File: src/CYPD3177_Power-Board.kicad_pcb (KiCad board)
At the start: 2 copper layers, 100 x 100 mm, 1 part

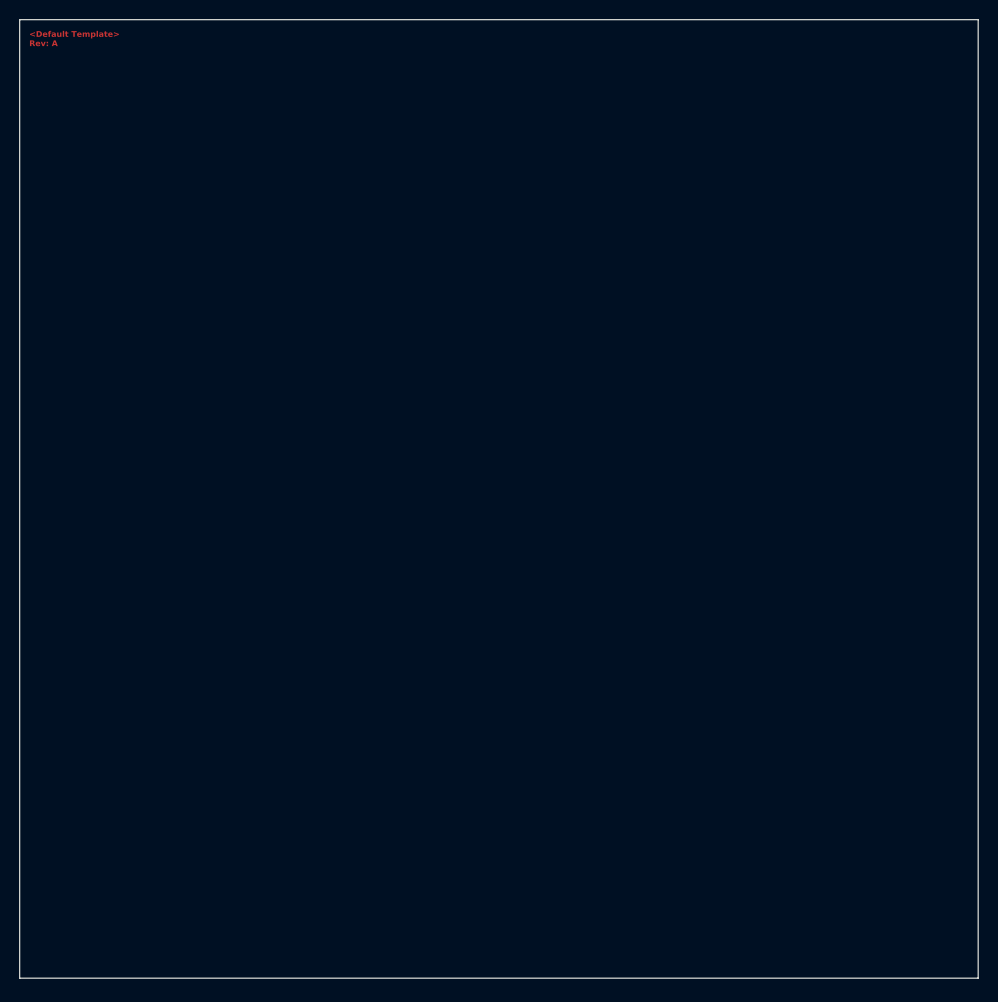
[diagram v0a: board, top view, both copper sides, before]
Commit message: Mod: PCB, placed components, draw board shape and placed a few traces
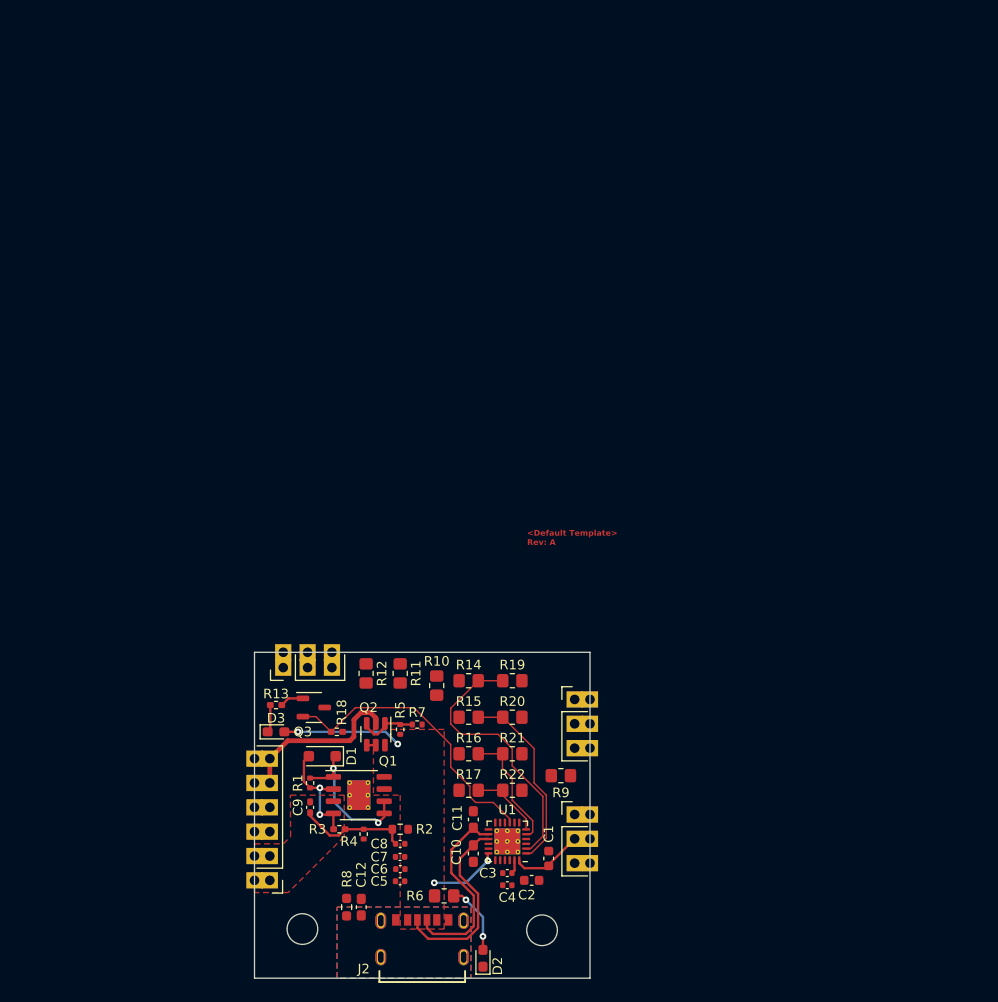
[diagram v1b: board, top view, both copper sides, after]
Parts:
- added C1: 1µF, Capacitor_SMD:C_0603_1608Metric, F.Cu at (155.2, 127.5)
- added C10: 390pF, Capacitor_SMD:C_0603_1608Metric_Pad1.08x0.95mm_HandSolder, F.Cu at (147.3, 127.0)
- added C11: 390pF, Capacitor_SMD:C_0603_1608Metric_Pad1.08x0.95mm_HandSolder, F.Cu at (147.3, 123.4)
- added C12: 4.7nF, Capacitor_SMD:C_0603_1608Metric_Pad1.08x0.95mm_HandSolder, F.Cu at (135.6, 132.6)
- added C2: 1µF, Capacitor_SMD:C_0603_1608Metric, F.Cu at (153.4, 129.8)
- added C3: 0.1µF, Capacitor_SMD:C_0402_1005Metric, F.Cu at (150.9, 129.0)
- added C4: 0.1µF, Capacitor_SMD:C_0402_1005Metric, F.Cu at (150.9, 130.3)
- added C5: 1µF, Capacitor_SMD:C_0402_1005Metric, F.Cu at (139.7, 129.9)
- added C6: 1µF, Capacitor_SMD:C_0402_1005Metric, F.Cu at (139.7, 128.6)
- added C7: 1µF, Capacitor_SMD:C_0402_1005Metric, F.Cu at (139.7, 127.3)
- added C8: 1µF, Capacitor_SMD:C_0402_1005Metric, F.Cu at (139.7, 126.0)
- added C9: 1µF, Capacitor_SMD:C_0402_1005Metric_Pad0.74x0.62mm_HandSolder, F.Cu at (130.3, 122.2)
- added D1: NZH10C,115, Diode_SMD:D_SOD-123F, F.Cu at (131.6, 116.8)
- added D2: LTST-C190GKT, LED_SMD:LED_0603_1608Metric_Pad1.05x0.95mm_HandSolder, F.Cu at (148.3, 137.9)
- added D3: LTST-C190EKT, LED_SMD:LED_0603_1608Metric_Pad1.05x0.95mm_HandSolder, F.Cu at (126.7, 114.3)
- added H1: MountingHole, MountingHole:MountingHole_3.2mm_M3, F.Cu at (129.5, 134.9)
- added H2: MountingHole, MountingHole:MountingHole_3.2mm_M3, F.Cu at (154.5, 135.0)
- added J1: Conn_01x06, Connector_CastellatedHole_2.54mm_User:CastellatedHole_1x06_P2.54mm_PinHeaders, F.Cu at (124.5, 129.8)
- added J2: USB4125-GF-A, Connector_User:GCT_USB4125-GF-A, F.Cu at (142.0, 137.0)
- added J3: Conn_01x03, Connector_CastellatedHole_2.54mm_User:CastellatedHole_1x03_P2.54mm_PinHeader, F.Cu at (159.5, 122.9)
- added J4: Conn_01x03, Connector_CastellatedHole_2.54mm_User:CastellatedHole_1x03_P2.54mm_PinHeader, F.Cu at (127.5, 106.0)
- added J5: Conn_01x03, Connector_CastellatedHole_2.54mm_User:CastellatedHole_1x03_P2.54mm_PinHeader, F.Cu at (159.5, 110.9)
- added Q1: IRF9358PbF, Package_SO:HSOP-8-1EP_3.9x4.9mm_P1.27mm_EP2.41x3.1mm_ThermalVias, F.Cu at (135.4, 120.9)
- added Q2: BSL308PE, Package_TO_SOT_SMD:SOT-23-6, F.Cu at (137.2, 114.6)
- added Q3: NTR4503N, Package_TO_SOT_SMD:SOT-23-3, F.Cu at (130.7, 111.8)
- added R1: 49.9kΩ, Resistor_SMD:R_0402_1005Metric, F.Cu at (130.3, 119.6)
- added R10: 2.2kΩ, Resistor_SMD:R_0805_2012Metric_Pad1.20x1.40mm_HandSolder, F.Cu at (143.5, 109.5)
- added R11: 2.2kΩ, Resistor_SMD:R_0805_2012Metric_Pad1.20x1.40mm_HandSolder, F.Cu at (139.7, 108.2)
- added R12: 2.2kΩ, Resistor_SMD:R_0805_2012Metric_Pad1.20x1.40mm_HandSolder, F.Cu at (136.1, 108.2)
- added R13: 1kΩ, Resistor_SMD:R_0402_1005Metric_Pad0.72x0.64mm_HandSolder, F.Cu at (126.7, 111.5)
- added R14: 5.1kΩ, Resistor_SMD:R_0805_2012Metric_Pad1.20x1.40mm_HandSolder, F.Cu at (146.8, 109.0)
- added R15: 5.1kΩ, Resistor_SMD:R_0805_2012Metric_Pad1.20x1.40mm_HandSolder, F.Cu at (146.8, 112.8)
- added R16: 5.1kΩ, Resistor_SMD:R_0805_2012Metric_Pad1.20x1.40mm_HandSolder, F.Cu at (146.8, 116.6)
- added R17: 5.1kΩ, Resistor_SMD:R_0805_2012Metric_Pad1.20x1.40mm_HandSolder, F.Cu at (146.8, 120.4)
- added R18: 49.9kΩ, Resistor_SMD:R_0402_1005Metric_Pad0.72x0.64mm_HandSolder, F.Cu at (133.1, 114.3)
- added R19: 5.1kΩ, Resistor_SMD:R_0805_2012Metric_Pad1.20x1.40mm_HandSolder, F.Cu at (151.4, 109.0)
- added R2: 10kΩ, Resistor_SMD:R_0603_1608Metric, F.Cu at (139.7, 124.5)
- added R20: 2.2kΩ, Resistor_SMD:R_0805_2012Metric_Pad1.20x1.40mm_HandSolder, F.Cu at (151.4, 112.8)
- added R21: 5.1kΩ, Resistor_SMD:R_0805_2012Metric_Pad1.20x1.40mm_HandSolder, F.Cu at (151.4, 116.6)
- added R22: 2.2kΩ, Resistor_SMD:R_0805_2012Metric_Pad1.20x1.40mm_HandSolder, F.Cu at (151.4, 120.4)
- added R3: 0Ω, Resistor_SMD:R_0402_1005Metric_Pad0.72x0.64mm_HandSolder, F.Cu at (133.3, 124.5)
- added R4: 1kΩ, Resistor_SMD:R_0402_1005Metric, F.Cu at (135.9, 125.0)
- added R5: 49.9kΩ, Resistor_SMD:R_0402_1005Metric, F.Cu at (139.7, 114.0)
- added R6: 2.2kΩ, Resistor_SMD:R_0805_2012Metric_Pad1.20x1.40mm_HandSolder, F.Cu at (144.3, 131.4)
- added R7: 1kΩ, Resistor_SMD:R_0402_1005Metric, F.Cu at (141.5, 113.5)
- added R8: 1M, Resistor_SMD:R_0603_1608Metric_Pad0.98x0.95mm_HandSolder, F.Cu at (134.1, 132.6)
- added R9: 2.2kΩ, Resistor_SMD:R_0805_2012Metric_Pad1.20x1.40mm_HandSolder, F.Cu at (156.5, 118.9)
- added U1: CYPD3177-24LQXQx, Package_DFN_QFN:QFN-24-1EP_4x4mm_P0.5mm_EP2.7x2.7mm_ThermalVias, F.Cu at (150.9, 125.7)
- moved G0 73.5 mm to (154.9, 98.0)
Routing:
- net /FAULT: track 0.00 -> 30.5 mm
- net /VBUS_{MAX}: track 0.00 -> 28.5 mm
- net /CC2: track 0.00 -> 20.4 mm
- net /VBUS: track 0.00 -> 20.1 mm, vias 0 -> 4
- net /CC1: track 0.00 -> 20.0 mm
- net /VBUS_{MIN}: track 0.00 -> 19.9 mm
- net /Safe-5V_{OUT}: track 0.00 -> 17.4 mm
- net /FET_{SRC}: track 0.00 -> 16.3 mm, vias 0 -> 2
- net /I_{Sink, Coarse}: track 0.00 -> 12.8 mm
- net /FET_{Gate}: track 0.00 -> 12.2 mm, vias 0 -> 2
- net Net-(C8-Pad2): track 0.00 -> 11.7 mm
- net /I_{Sink, Fine}: track 0.00 -> 7.65 mm
- net +1V8: track 0.00 -> 7.63 mm
- net Net-(D2-A): track 0.00 -> 7.40 mm, vias 0 -> 2
- net Net-(Q2-Pad1): track 0.00 -> 6.20 mm
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- added copper zone on F.Cu, net /DC_{OUT}
- added copper zone on B.Cu, net /Shield
- added copper zone on F.Cu, net /Shield
- added copper zone on F.Cu, net /VBUS
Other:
- board size 100 x 100 mm -> 35 x 34 mm

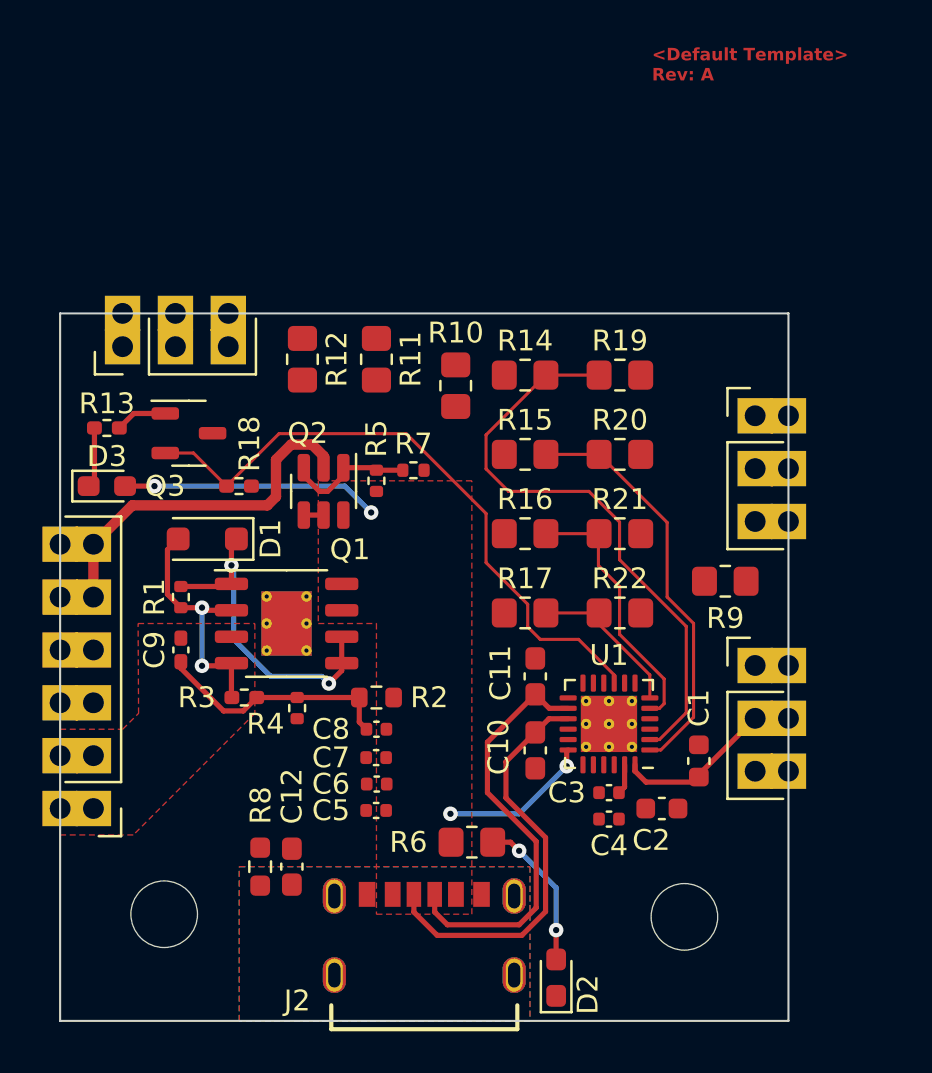
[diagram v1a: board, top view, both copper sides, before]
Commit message: Mod: Moved voltage dividers and placed all traces
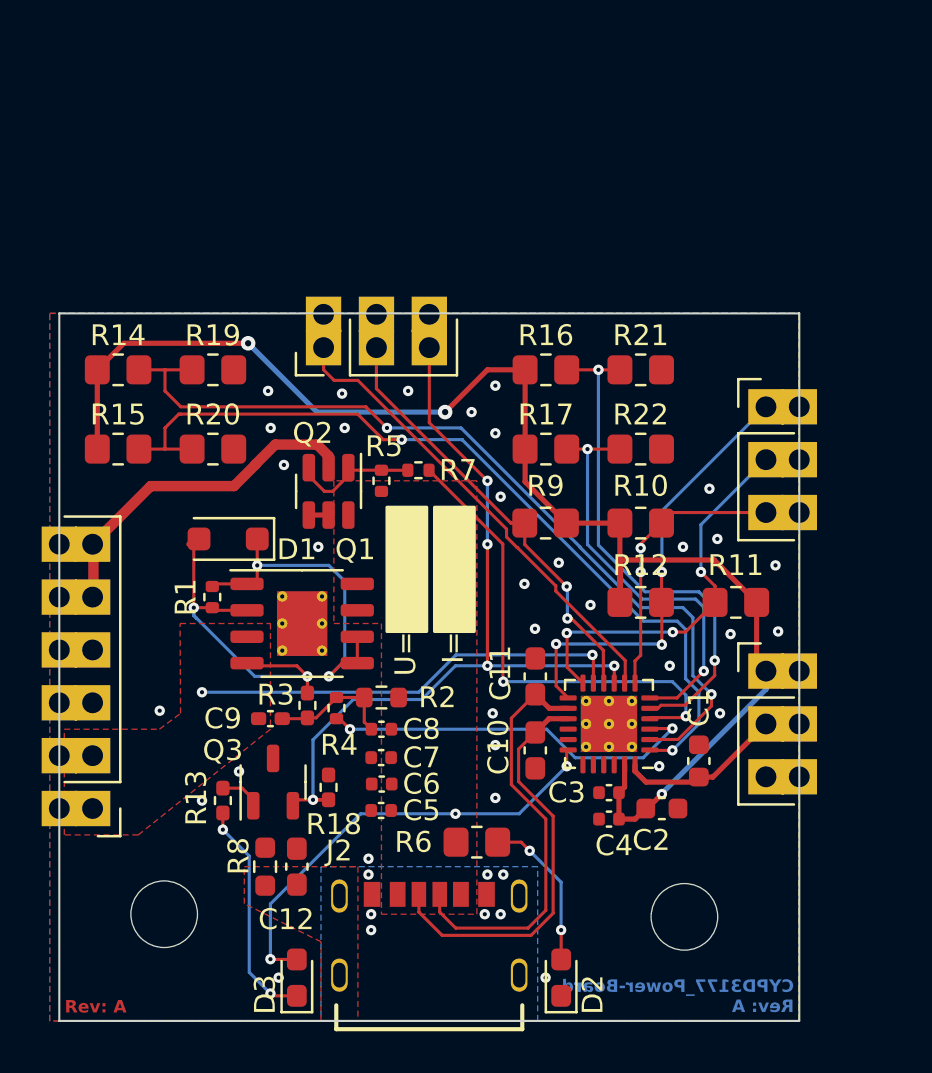
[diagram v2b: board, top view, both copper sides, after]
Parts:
- moved J4 32.8 mm to (160.0, 110.5), turned to 0 degrees
- moved D3 25.3 mm to (135.9, 137.9), turned to 90 degrees
- moved J5 22.9 mm to (137.2, 106.0), turned to 90 degrees
- moved R11 20.9 mm to (157.0, 119.9), turned to 180 degrees
- moved R12 20.0 mm to (152.4, 119.9), turned to 0 degrees
- moved R14 19.6 mm to (127.3, 108.7)
- moved R15 19.6 mm to (127.3, 112.5)
- moved R19 19.6 mm to (131.8, 108.7)
- moved R20 19.6 mm to (131.8, 112.5)
- moved R13 18.8 mm to (132.3, 129.4), turned to 90 degrees
- moved Q3 17.2 mm to (134.7, 128.5), turned to 90 degrees
- moved R18 15.1 mm to (137.4, 128.8), turned to 90 degrees
- moved R10 11.1 mm to (152.4, 116.1), turned to 0 degrees
- moved G0 9.86 mm to (156.2, 107.8), turned to 90 degrees
- moved R9 9.08 mm to (147.8, 116.1)
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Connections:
- Q1 pad 9: (no net) -> GND
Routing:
- net +3V3: track 1.45 -> 67.9 mm, vias 0 -> 3
- net Net-(U1-SAFE_PWR_EN): track 0.00 -> 23.5 mm, vias 0 -> 2
- net /GPIO: track 0.00 -> 22.8 mm
- net /SCL: track 0.00 -> 21.4 mm, vias 0 -> 3
- net /FLIP: track 0.00 -> 21.2 mm, vias 0 -> 2
- net /VBUS_{MIN}: track 19.9 -> 40.9 mm, vias 0 -> 2
- net /DC_{OUT}: track 0.00 -> 20.9 mm, vias 0 -> 2
- net /SDA: track 0.00 -> 18.9 mm, vias 0 -> 3
- net Net-(U1-VBUS_FET_EN): track 0.00 -> 18.6 mm, vias 0 -> 2
- net /~{INT}: track 0.00 -> 13.4 mm, vias 0 -> 2
- net /VBUS_{MAX}: track 28.5 -> 41.7 mm, vias 0 -> 2
- net /I_{Sink, Fine}: track 7.65 -> 20.2 mm, vias 0 -> 2
- net /I_{Sink, Coarse}: track 12.8 -> 24.8 mm, vias 0 -> 2
- net /FAULT: track 30.5 -> 38.7 mm, vias 0 -> 5
- net Net-(D3-K): track 2.91 -> 10.9 mm, vias 0 -> 2
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- added copper zone on B.Cu, net GND
- added copper zone on F.Cu, net GND
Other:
- board size 35 x 34 mm -> 35.6 x 34 mm
- board text added: "I="
- board text added: "Rev: ${REVISION}"
- board text added: "U="

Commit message: Mod: PCB, last touches, moved logo, added some more vias and some pin labels
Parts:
- moved C2 40.2 mm to (149.0, 89.8)
- moved C3 40.2 mm to (146.4, 89.0)
- moved J1 40.2 mm to (120.0, 89.8)
- moved R13 40.2 mm to (127.9, 89.4)
- moved C1 40.2 mm to (150.7, 87.5)
- moved C10 40.2 mm to (142.9, 87.0)
- moved C11 40.2 mm to (142.9, 83.4)
- moved C12 40.2 mm to (131.4, 92.6)
- moved C5 40.2 mm to (135.5, 89.9)
- moved C6 40.2 mm to (135.5, 88.6)
- moved C7 40.2 mm to (135.5, 87.3)
- moved C8 40.2 mm to (135.5, 86.0)
- moved C9 40.2 mm to (130.1, 85.5)
- moved D1 40.2 mm to (128.1, 76.8)
- moved D2 40.2 mm to (144.1, 97.9)
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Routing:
- net GND: vias 40 -> 44
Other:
- board text added: "+1V8"
- board text added: "+3V3"
- board text added: "5V_{OUT}"
- board text added: "DC_{OUT}"
- board text added: "FAULT"
- board text added: "FLIP"
- board text added: "GND"
- board text added: "GPIO"
- board text added: "SCL"
- board text added: "SDA"
- board text added: "~{INT}"

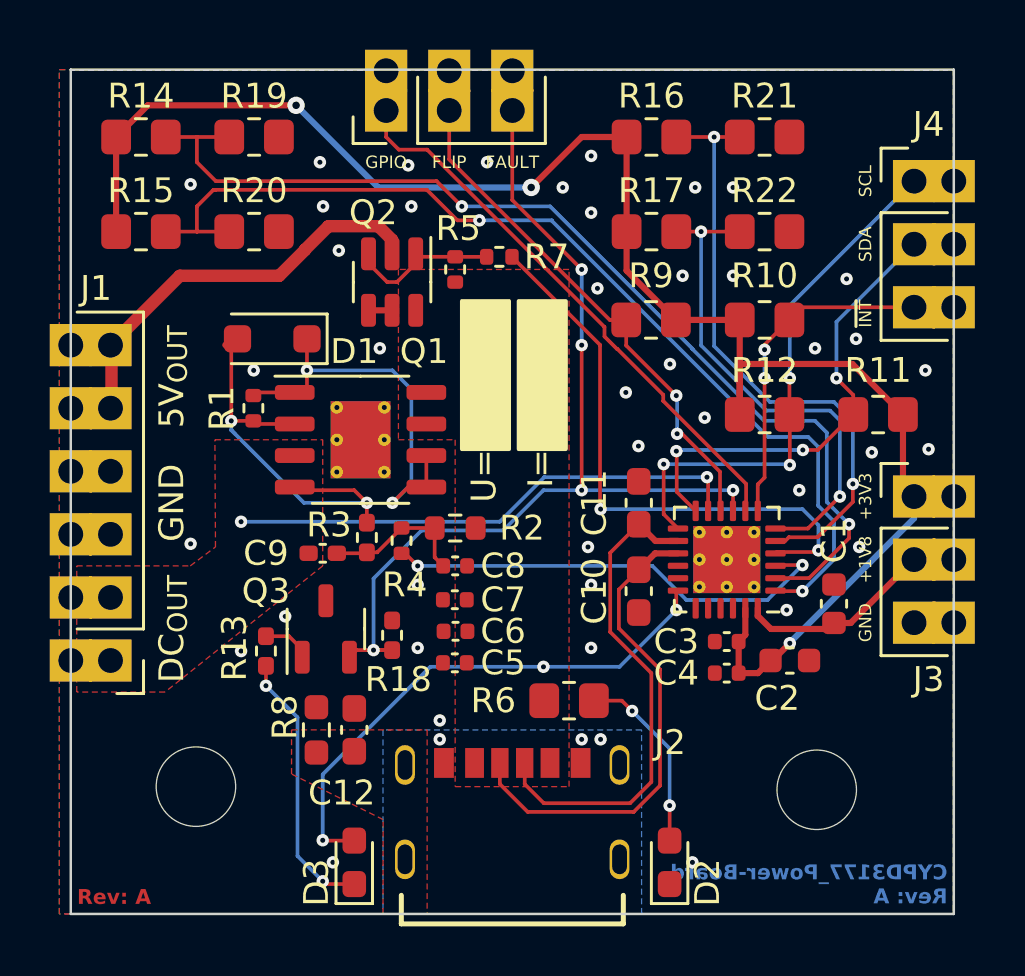
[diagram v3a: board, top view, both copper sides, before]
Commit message: Add: Dimensions and moved holes and castellated holes
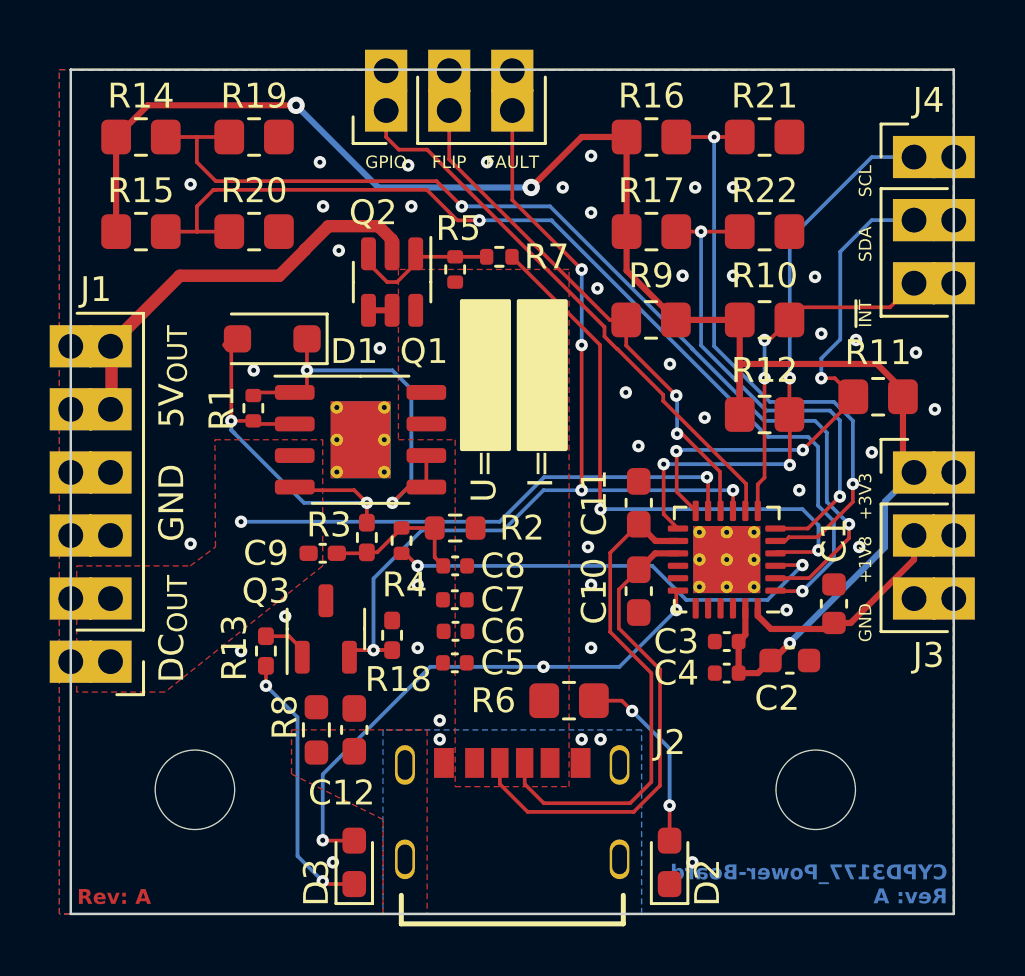
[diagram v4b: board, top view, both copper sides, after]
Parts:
- moved J3 0.97 mm to (155.6, 82.2)
- moved J4 0.97 mm to (155.6, 69.5)
- moved R11 0.72 mm to (152.5, 79.2)
- moved H1 0.13 mm to (125.0, 95.0)
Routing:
- net /SDA: track 18.9 -> 21.3 mm
- net /SCL: track 21.4 -> 23.4 mm
- net +1V8: track 7.97 -> 8.94 mm
- net +3V3: track 67.9 -> 68.5 mm
- net /~{INT}: track 13.4 -> 14.0 mm
